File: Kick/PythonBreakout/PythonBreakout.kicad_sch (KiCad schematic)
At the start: 17 parts, among them J1 Conn_01x12, J2 Conn_01x12, J3 Conn_01x12, J4 Conn_01x12, U0 NOIP1SN1300A-QTI

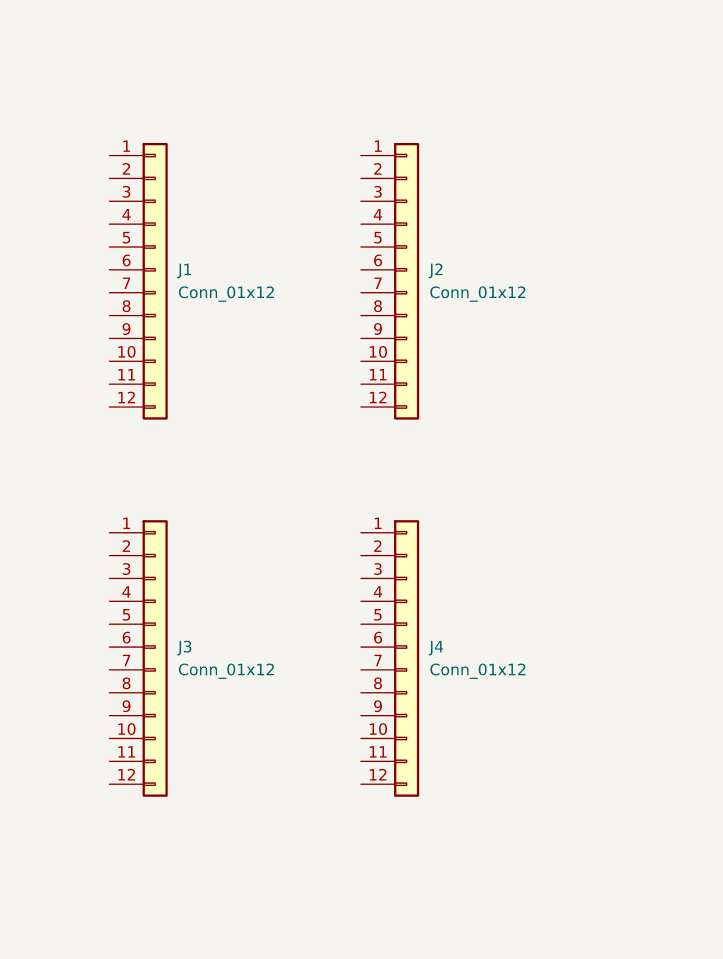
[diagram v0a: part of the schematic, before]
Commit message: tried several connectors, chose TFML/SFML. routing LVDS witb 0 skew.
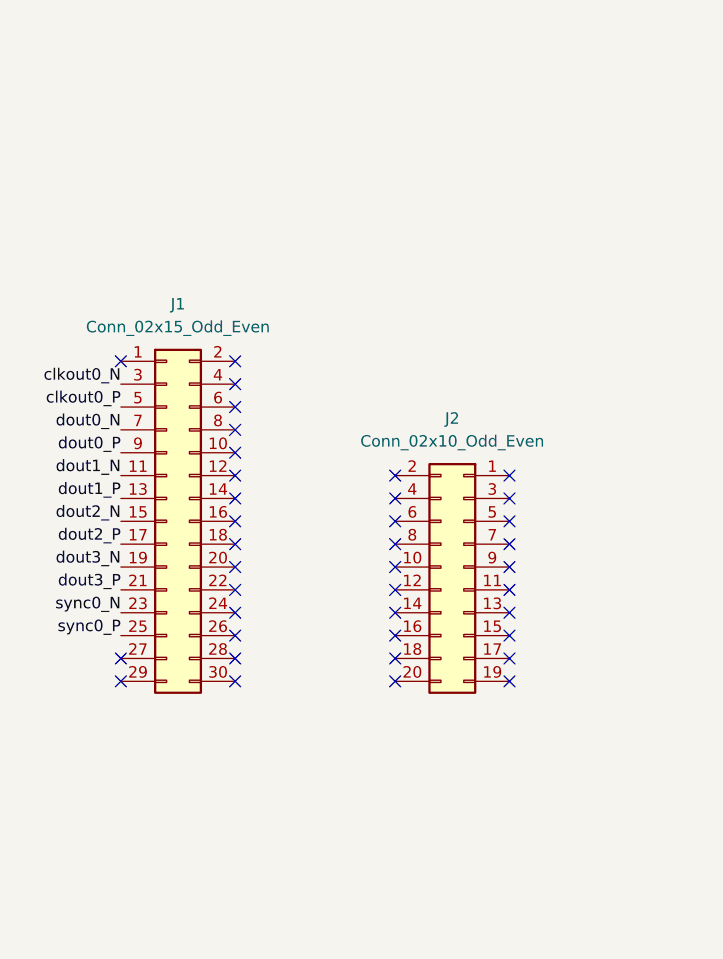
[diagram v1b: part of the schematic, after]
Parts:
- removed J1, J2, J3, J4: Conn_01x12, symbol Connector_Generic:Conn_01x12
- added J1: Conn_02x15_Odd_Even, SAMTEC_SFML11502LDLC:SAMTEC_SFML-115-02-L-D-LC, symbol Connector_Generic:Conn_02x15_Odd_Even
- added J2: Conn_02x10_Odd_Even, SAMTEC_SFML11002LDLC:SAMTEC_SFML-110-02-L-D-LC, symbol Connector_Generic:Conn_02x10_Odd_Even
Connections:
- net clkout0_N: now also J1.3 (Pin_3)
- net clkout0_P: now also J1.5 (Pin_5)
- net dout0_N: now also J1.7 (Pin_7)
- net dout0_P: now also J1.9 (Pin_9)
- net dout1_N: now also J1.11 (Pin_11)
- net dout1_P: now also J1.13 (Pin_13)
- net dout2_N: now also J1.15 (Pin_15)
- net dout2_P: now also J1.17 (Pin_17)
- net dout3_N: now also J1.19 (Pin_19)
- net dout3_P: now also J1.21 (Pin_21)
- net sync0_N: now also J1.23 (Pin_23)
- net sync0_P: now also J1.25 (Pin_25)
- no-connect marks 4 -> 42

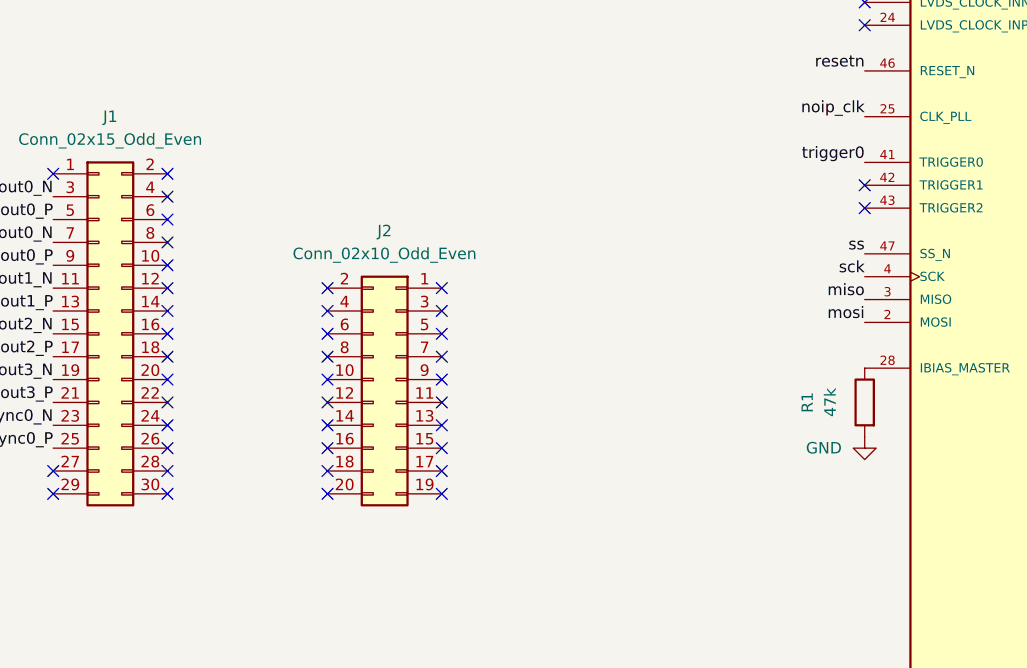
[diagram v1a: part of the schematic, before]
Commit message: routed PythonBreakout with SFML
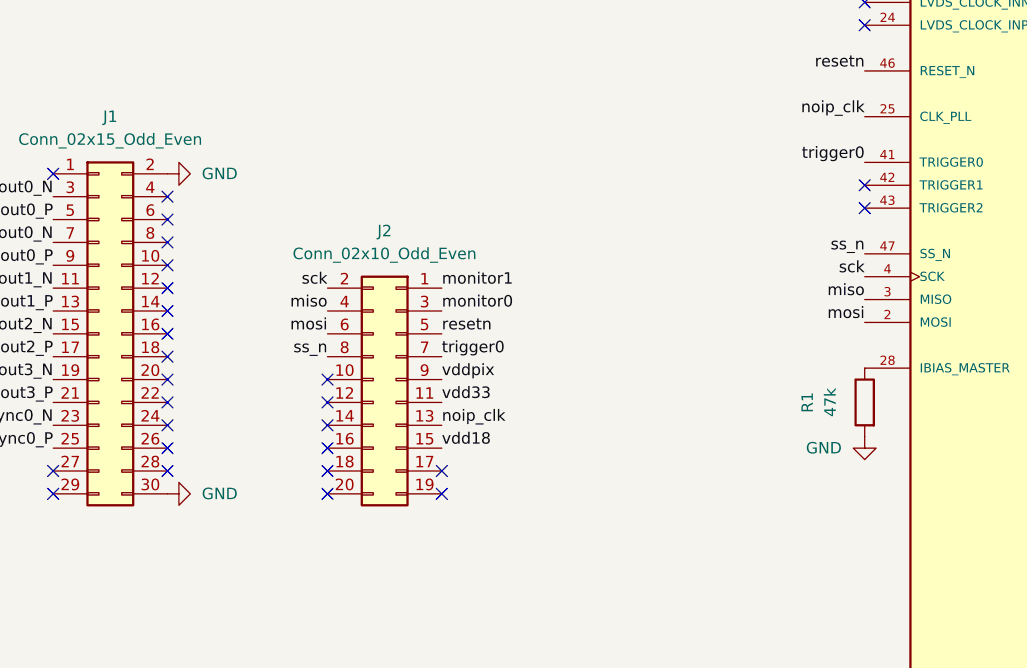
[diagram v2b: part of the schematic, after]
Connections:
- net ss is gone; now on net ss_n: U0.47 (SS_N)
- net GND: now also J1.2 (Pin_2), J1.30 (Pin_30)
- net miso: now also J2.4 (Pin_4)
- net monitor0: now also J2.3 (Pin_3)
- net monitor1: now also J2.1 (Pin_1)
- net mosi: now also J2.6 (Pin_6)
- net noip_clk: now also J2.13 (Pin_13)
- net resetn: now also J2.5 (Pin_5)
- net sck: now also J2.2 (Pin_2)
- net trigger0: now also J2.7 (Pin_7)
- net vdd18: now also J2.15 (Pin_15)
- net vdd33: now also J2.11 (Pin_11)
- net vddpix: now also J2.9 (Pin_9)
- net ss_n: now reaches J2.8 (Pin_8)
- no-connect marks 42 -> 28

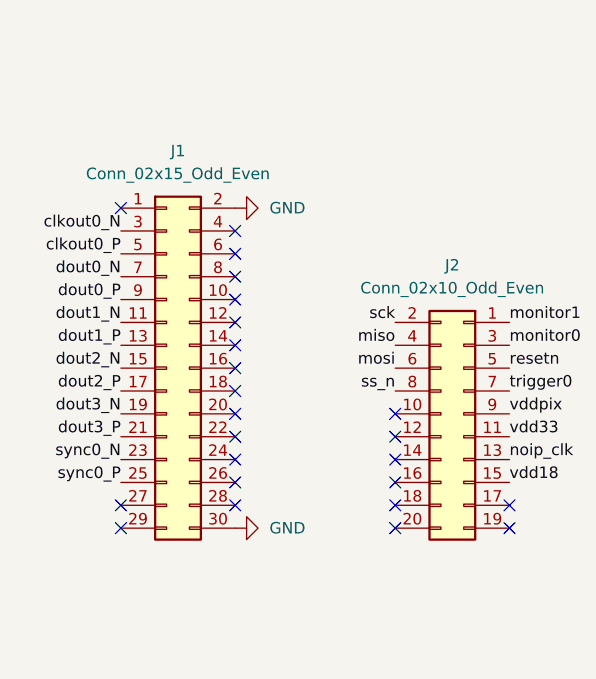
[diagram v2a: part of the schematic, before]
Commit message: routed 0 side on MainBoard with TFMLs
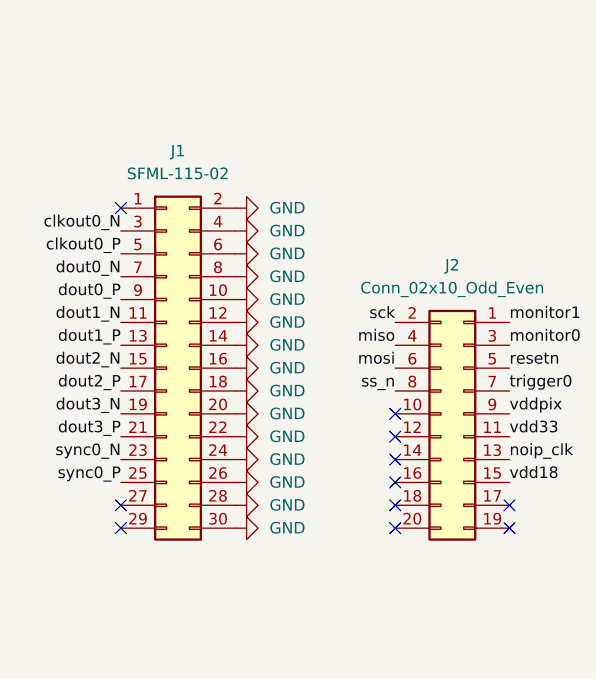
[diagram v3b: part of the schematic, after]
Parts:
- J1: value Conn_02x15_Odd_Even -> SFML-115-02
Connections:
- net GND: now also J1.10 (Pin_10), J1.12 (Pin_12), J1.14 (Pin_14), J1.16 (Pin_16), J1.18 (Pin_18), J1.20 (Pin_20), J1.22 (Pin_22), J1.24 (Pin_24), J1.26 (Pin_26), J1.28 (Pin_28), J1.4 (Pin_4), J1.6 (Pin_6), J1.8 (Pin_8)
- no-connect marks 28 -> 15

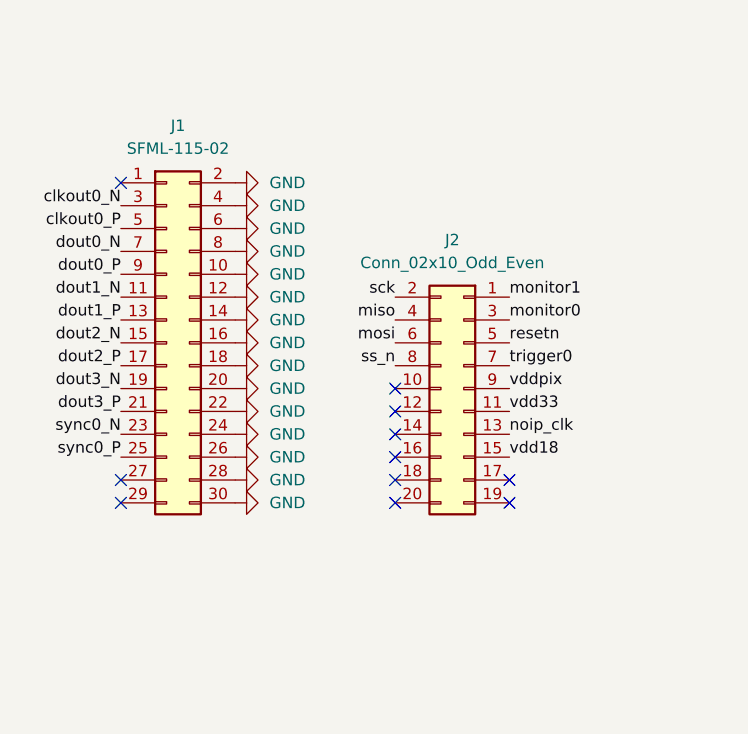
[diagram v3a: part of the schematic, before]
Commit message: routed all layers, length matched top part and updated models
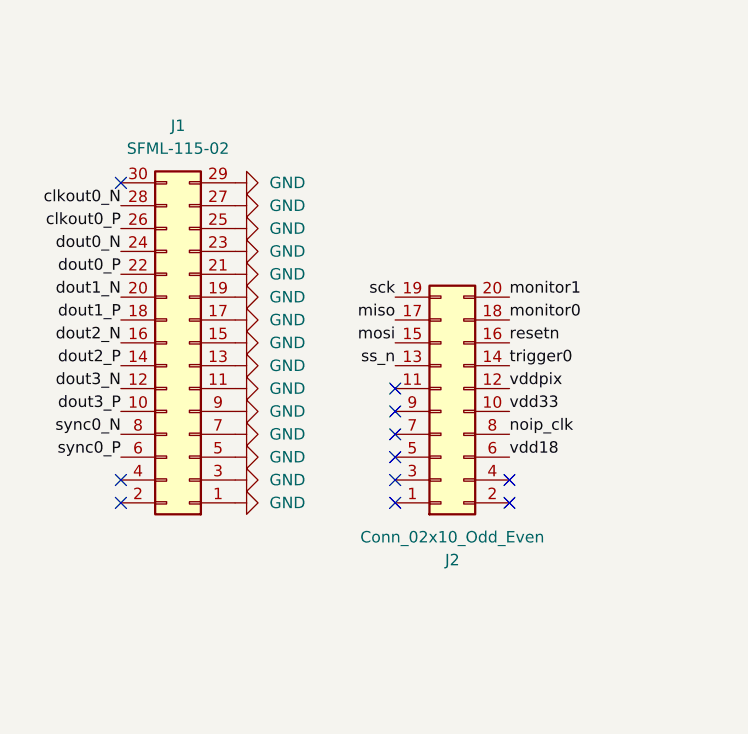
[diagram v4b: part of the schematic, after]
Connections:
- net GND: now also J1.1 (Pin_1), J1.11 (Pin_11), J1.13 (Pin_13), J1.15 (Pin_15), J1.17 (Pin_17), J1.19 (Pin_19), J1.21 (Pin_21), J1.23 (Pin_23), J1.25 (Pin_25), J1.27 (Pin_27), J1.29 (Pin_29), J1.3 (Pin_3), J1.5 (Pin_5), J1.7 (Pin_7), J1.9 (Pin_9); no longer J1.10 (Pin_10), J1.12 (Pin_12), J1.14 (Pin_14), J1.16 (Pin_16), J1.18 (Pin_18), J1.2 (Pin_2), J1.20 (Pin_20), J1.22 (Pin_22), J1.24 (Pin_24), J1.26 (Pin_26), J1.28 (Pin_28), J1.30 (Pin_30), J1.4 (Pin_4), J1.6 (Pin_6), J1.8 (Pin_8)
- net clkout0_N: now also J1.28 (Pin_28); no longer J1.3 (Pin_3)
- net clkout0_P: now also J1.26 (Pin_26); no longer J1.5 (Pin_5)
- net dout0_N: now also J1.24 (Pin_24); no longer J1.7 (Pin_7)
- net dout0_P: now also J1.22 (Pin_22); no longer J1.9 (Pin_9)
- net dout1_N: now also J1.20 (Pin_20); no longer J1.11 (Pin_11)
- net dout1_P: now also J1.18 (Pin_18); no longer J1.13 (Pin_13)
- net dout2_N: now also J1.16 (Pin_16); no longer J1.15 (Pin_15)
- net dout2_P: now also J1.14 (Pin_14); no longer J1.17 (Pin_17)
- net dout3_N: now also J1.12 (Pin_12); no longer J1.19 (Pin_19)
- net dout3_P: now also J1.10 (Pin_10); no longer J1.21 (Pin_21)
- net miso: now also J2.17 (Pin_17); no longer J2.4 (Pin_4)
- net monitor0: now also J2.18 (Pin_18); no longer J2.3 (Pin_3)
- net monitor1: now also J2.20 (Pin_20); no longer J2.1 (Pin_1)
- net mosi: now also J2.15 (Pin_15); no longer J2.6 (Pin_6)
- net noip_clk: now also J2.8 (Pin_8); no longer J2.13 (Pin_13)
- net resetn: now also J2.16 (Pin_16); no longer J2.5 (Pin_5)
- net sck: now also J2.19 (Pin_19); no longer J2.2 (Pin_2)
- net ss_n: now also J2.13 (Pin_13); no longer J2.8 (Pin_8)
- net sync0_N: now also J1.8 (Pin_8); no longer J1.23 (Pin_23)
- net sync0_P: now also J1.6 (Pin_6); no longer J1.25 (Pin_25)
- net trigger0: now also J2.14 (Pin_14); no longer J2.7 (Pin_7)
- net vdd18: now also J2.6 (Pin_6); no longer J2.15 (Pin_15)
- net vdd33: now also J2.10 (Pin_10); no longer J2.11 (Pin_11)
- net vddpix: now also J2.12 (Pin_12); no longer J2.9 (Pin_9)
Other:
- moved on the sheet: J1
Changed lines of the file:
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@@
 	(symbol
 		(lib_id "Connector_Generic:Conn_02x15_Odd_Even")
-		(at 40.64 76.2 0)
+		(at 43.18 76.2 180)
 		(unit 1)
 		(exclude_from_sim no)
@@
 		)
 		(property "Footprint" "SAMTEC_SFML11502LDLC:SAMTEC_SFML-115-02-L-D-LC"
-			(at 40.64 76.2 0)
+			(at 43.18 76.2 0)
 			(effects
 				(font
@@
 		)
 		(property "Datasheet" "~"
-			(at 40.64 76.2 0)
+			(at 43.18 76.2 0)
 			(effects
 				(font
@@
 		)
 		(property "Description" "Generic connector, double row, 02x15, odd/even pin numbering scheme (row 1 odd numbers, row 2 even numbers), script generated (kicad-library-utils/schlib/autogen/connector/)"
-			(at 40.64 76.2 0)
+			(at 43.18 76.2 0)
 			(effects
 				(font
@@
 	(symbol
 		(lib_id "Connector_Generic:Conn_02x10_Odd_Even")
-		(at 73.66 81.28 0)
-		(mirror y)
+		(at 71.12 83.82 0)
+		(mirror x)
 		(unit 1)
 		(exclude_from_sim no)
@@
 		(dnp no)
 		(property "Reference" "J2"
-			(at 72.39 64.77 0)
+			(at 72.39 100.33 0)
 			(effects
 				(font
@@
 		)
 		(property "Value" "Conn_02x10_Odd_Even"
-			(at 72.39 67.31 0)
+			(at 72.39 97.79 0)
 			(effects
 				(font
@@
 		)
 		(property "Footprint" "SAMTEC_SFML11002LDLC:SAMTEC_SFML-110-02-L-D-LC"
-			(at 73.66 81.28 0)
+			(at 71.12 83.82 0)
 			(effects
 				(font
@@
 		)
 		(property "Datasheet" "~"
-			(at 73.66 81.28 0)
+			(at 71.12 83.82 0)
 			(effects
 				(font
@@
 		)
 		(property "Description" "Generic connector, double row, 02x10, odd/even pin numbering scheme (row 1 odd numbers, row 2 even numbers), script generated (kicad-library-utils/schlib/autogen/connector/)"
-			(at 73.66 81.28 0)
-			(effects
-				(font
+			(at 71.12 83.82 0)
+			(effects
+				(font

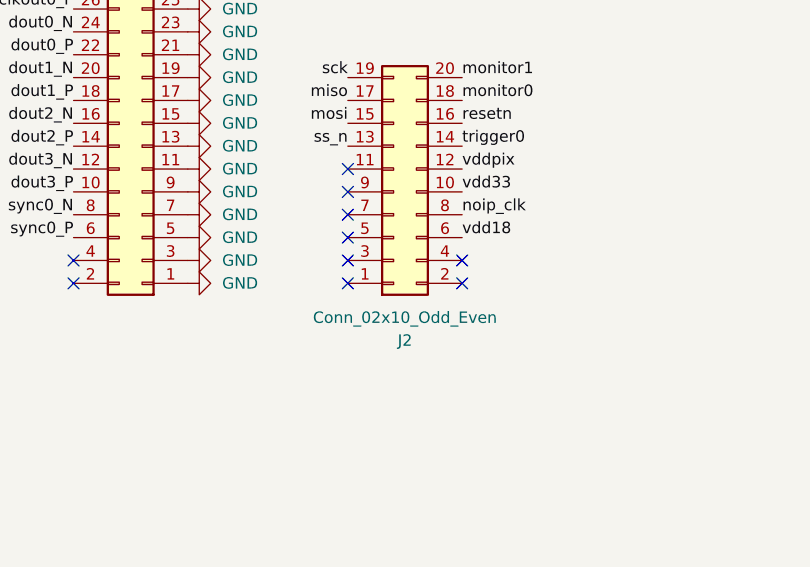
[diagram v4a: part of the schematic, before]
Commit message: verificated and generated output products for both boards
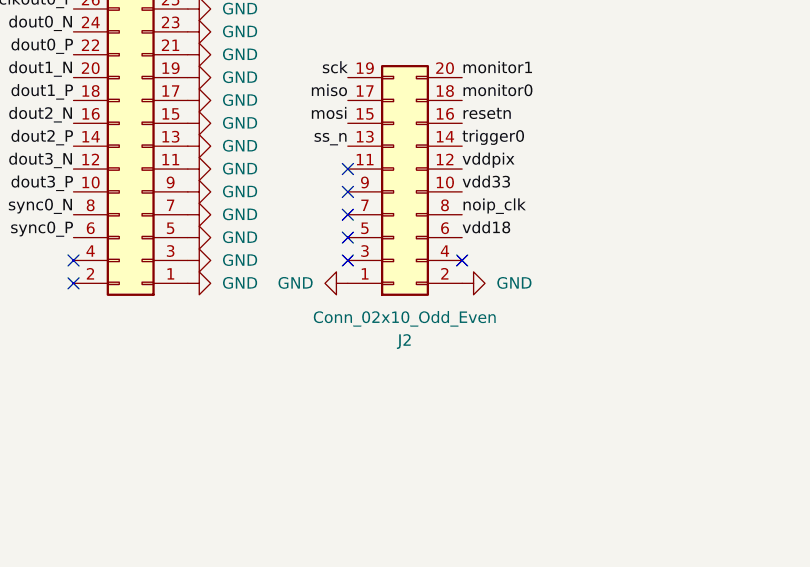
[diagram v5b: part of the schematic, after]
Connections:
- net GND: now also J2.1 (Pin_1), J2.2 (Pin_2)
- no-connect marks 15 -> 13
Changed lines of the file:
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@@
 	)
 	(no_connect
-		(at 78.74 93.98)
-	)
-	(no_connect
 		(at 66.04 88.9)
 	)
@@
 	)
 	(no_connect
-		(at 66.04 93.98)
-	)
-	(no_connect
 		(at 125.73 39.37)
 	)
@@
 	(symbol
 		(lib_id "power:GND")
+		(at 66.04 93.98 270)
+		(unit 1)
+		(exclude_from_sim no)
+		(in_bom yes)
+		(on_board yes)
+		(dnp no)
+		(fields_autoplaced yes)
+		(property "Reference" "#PWR028"
+			(at 59.69 93.98 0)
+			(effects
+				(font
+					(size 1.27 1.27)
+				)
+				(hide yes)
+			)
+		)
+		(property "Value" "GND"
+			(at 62.23 93.9799 90)
+			(effects
+				(font
+					(size 1.27 1.27)
+				)
+				(justify right)
+			)
+		)
+		(property "Footprint" ""
+			(at 66.04 93.98 0)
+			(effects
+				(font
+					(size 1.27 1.27)
+				)
+				(hide yes)
+			)
+		)
+		(property "Datasheet" ""
+			(at 66.04 93.98 0)
+			(effects
+				(font
+					(size 1.27 1.27)
+				)
+				(hide yes)
+			)
+		)
+		(property "Description" "Power symbol creates a global label with name \"GND\" , ground"
+			(at 66.04 93.98 0)
+			(effects
+				(font
+					(size 1.27 1.27)
+				)
+				(hide yes)
+			)
+		)
+		(pin "1"
+		)
+		(instances
+			(project "PythonBreakout"
+				(path "/277e05da-ccda-4679-9933-a39aa09eccc2"
+					(reference "#PWR028")
+					(unit 1)
+				)
+			)
+		)
+	)
+	(symbol
+		(lib_id "power:GND")
 		(at 48.26 83.82 90)
 		(unit 1)
@@
 					(unit 1)
 				)
+			)
+		)
+	)
+	(symbol
+		(lib_id "power:GND")
+		(at 78.74 93.98 90)
+		(unit 1)
+		(exclude_from_sim no)
+		(in_bom yes)
+		(on_board yes)
+		(dnp no)
+		(fields_autoplaced yes)
+		(property "Reference" "#PWR029"
+			(at 85.09 93.98 0)
+			(effects
+				(font
+					(size 1.27 1.27)
+				)
+				(hide yes)
+			)
+		)
+		(property "Value" "GND"
+			(at 82.55 93.9799 90)
+			(effects
+				(font
+					(size 1.27 1.27)
+				)
+				(justify right)
+			)
+		)
+		(property "Footprint" ""
+			(at 78.74 93.98 0)
+			(effects
+				(font
+					(size 1.27 1.27)
+				)
+				(hide yes)
+			)
+		)
+		(property "Datasheet" ""
+			(at 78.74 93.98 0)
+			(effects
+				(font
+					(size 1.27 1.27)
+				)
+				(hide yes)
+			)
+		)
+		(property "Description" "Power symbol creates a global label with name \"GND\" , ground"
+			(at 78.74 93.98 0)
+			(effects
+				(font
+					(size 1.27 1.27)
+				)
+				(hide yes)
+			)
+		)
+		(pin "1"
+		)
+		(instances
+			(project "PythonBreakout"
+				(path "/277e05da-ccda-4679-9933-a39aa09eccc2"
+					(reference "#PWR029")
+					(unit 1)
+				)
